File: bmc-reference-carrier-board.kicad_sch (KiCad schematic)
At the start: 0 parts

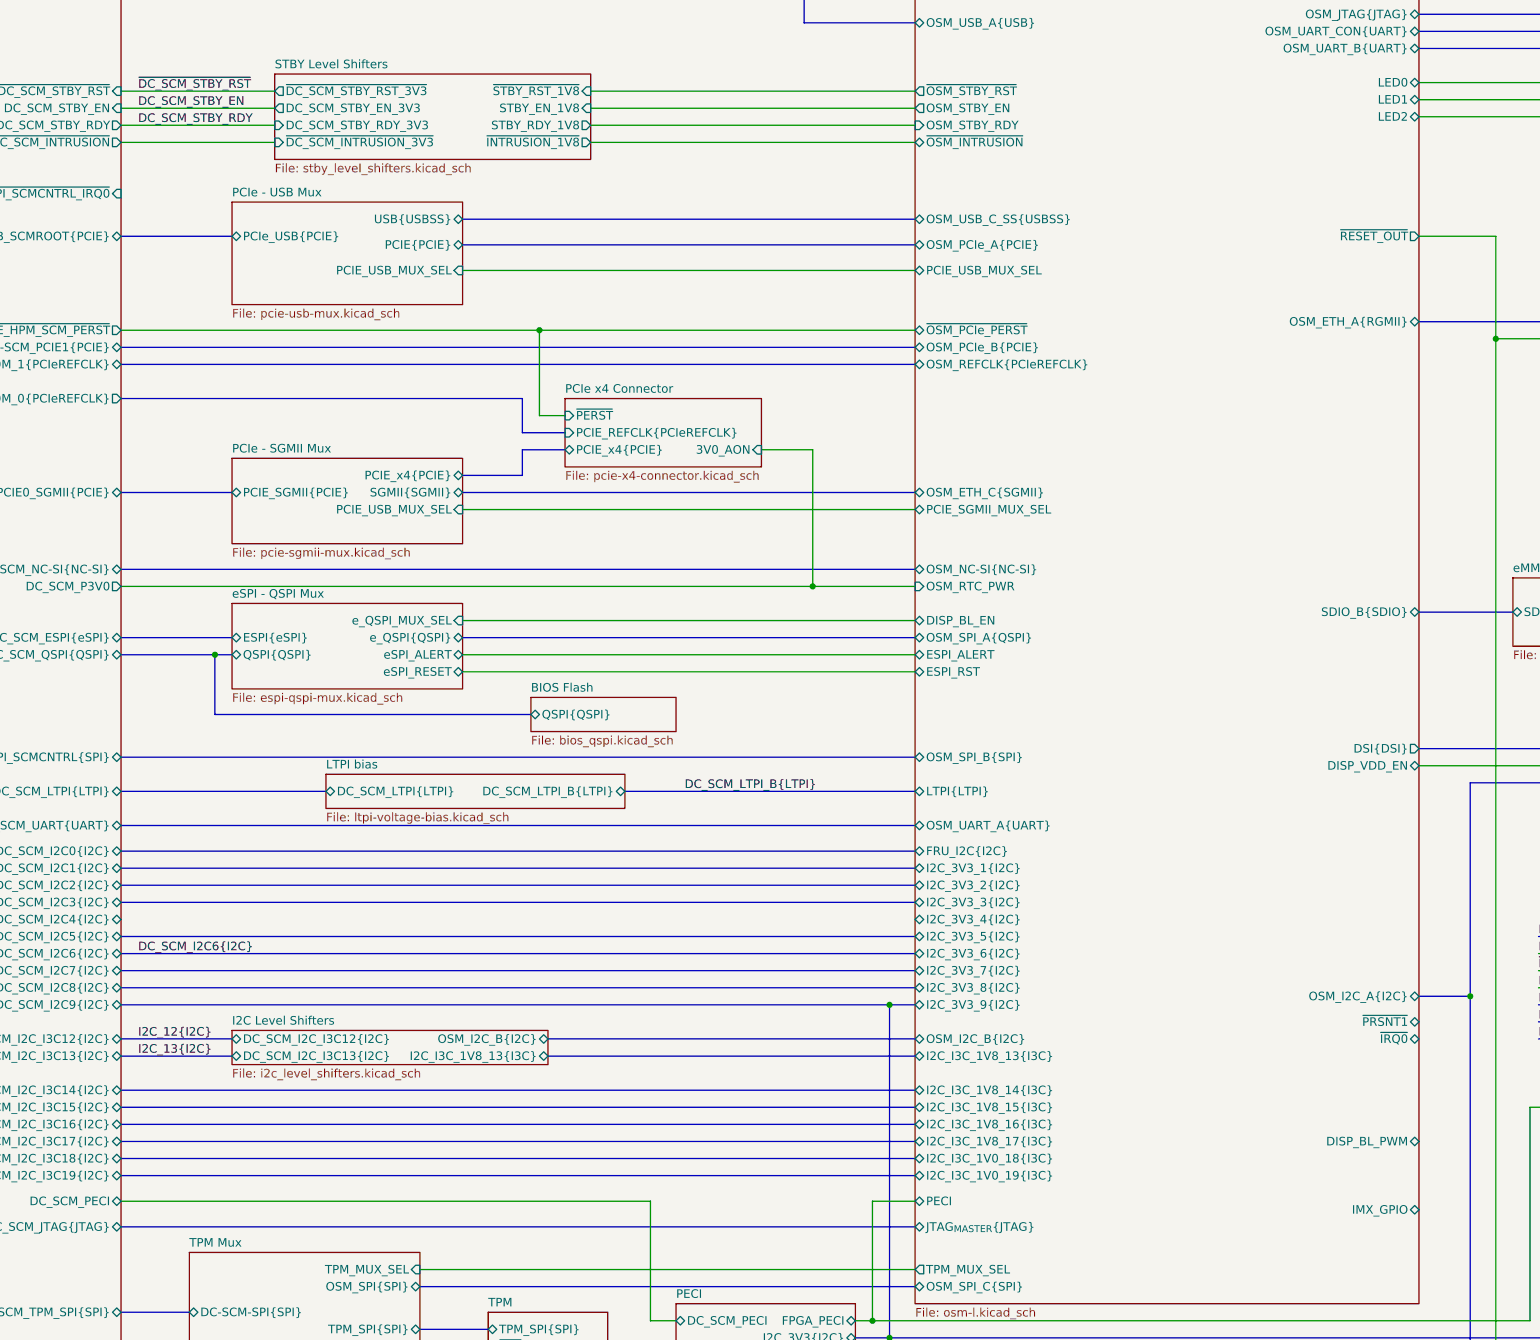
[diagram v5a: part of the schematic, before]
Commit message: [#83609] Add power pushbutton
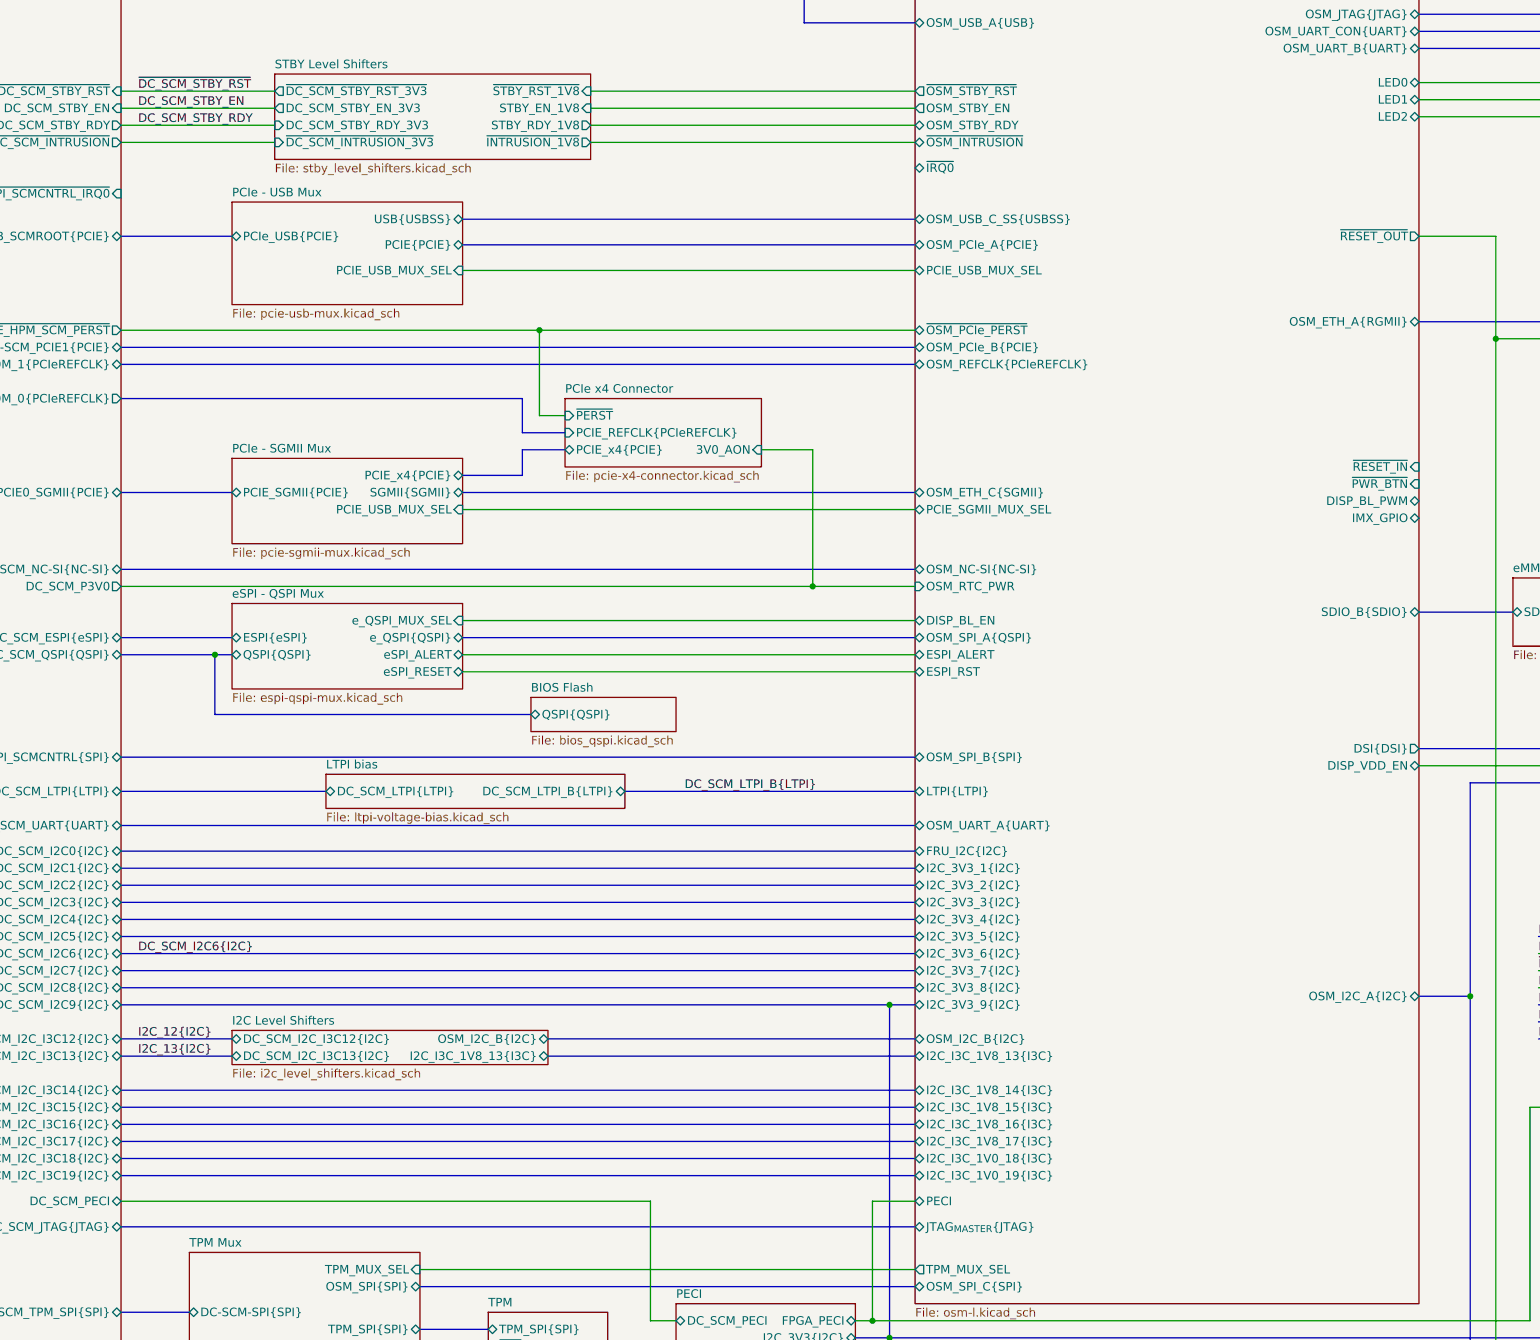
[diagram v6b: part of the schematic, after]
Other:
- sheet OSM L ports: added ~{PWR_BTN}, ~{RESET_IN}; removed ~{PRSNT1}
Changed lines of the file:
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@@
+	(bus
+		(pts
+			(xy 58.42 212.09) (xy 176.53 212.09)
+		)
+		(stroke
+			(width 0)
+			(type default)
+		)
+	)
 	(bus
 		(pts
@@
 			)
 		)
-		(pin "OSM_STBY_RDY" input
-			(at 176.53 93.98 180)
-			(effects
-				(font
-					(size 1.27 1.27)
-				)
-				(justify left)
-			)
-		)
 		(pin "~{OSM_INTRUSION}" bidirectional
 			(at 176.53 96.52 180)
@@
 		)
 		(pin "DISP_BL_PWM" bidirectional
-			(at 251.46 245.11 0)
+			(at 251.46 149.86 0)
 			(effects
 				(font
@@
 		)
 		(pin "IMX_GPIO" bidirectional
-			(at 251.46 255.27 0)
+			(at 251.46 152.4 0)
 			(effects
 				(font
@@
 		)
 		(pin "~{IRQ0}" bidirectional
-			(at 251.46 229.87 0)
-			(effects
-				(font
-					(size 1.27 1.27)
-				)
-				(justify right)
-			)
-		)
-		(pin "~{PRSNT1}" bidirectional
-			(at 251.46 227.33 0)
-			(effects
-				(font
-					(size 1.27 1.27)
-				)
-				(justify right)
+			(at 176.53 100.33 180)
+			(effects
+				(font
+					(size 1.27 1.27)
+				)
+				(justify left)
 			)
 		)
@@
 			(effects
 				(font
+					(size 1.27 1.27)
+				)
+				(justify right)
+			)
+		)
+		(pin "~{PWR_BTN}" input
+			(at 251.46 147.32 0)
+			(effects
+				(font
+					(size 1.27 1.27)
+				)
+				(justify right)
+			)
+		)
+		(pin "OSM_STBY_RDY" bidirectional
+			(at 176.53 93.98 180)
+			(effects
+				(font
+					(size 1.27 1.27)
+				)
+				(justify left)
+			)
+		)
+		(pin "~{RESET_IN}" input
+			(at 251.46 144.78 0)
+			(effects
+				(font

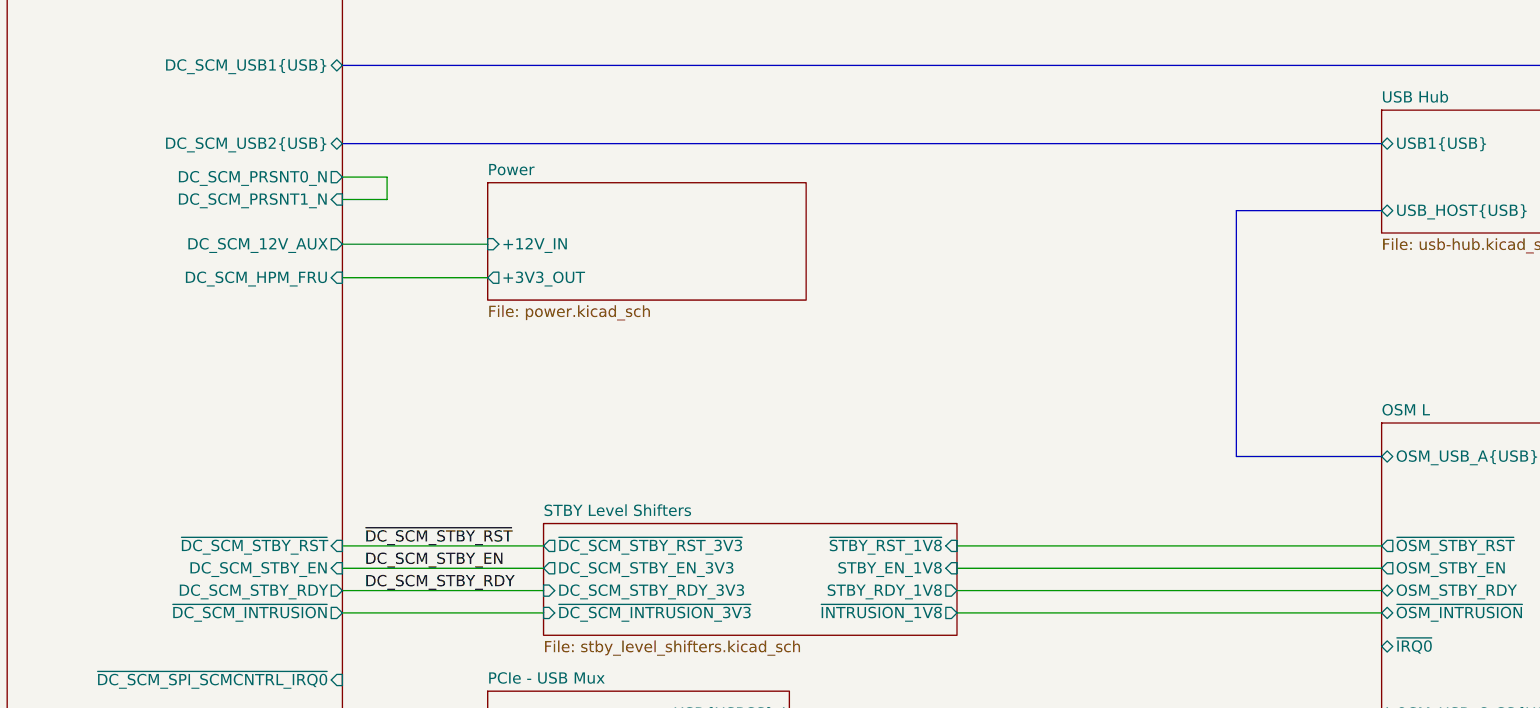
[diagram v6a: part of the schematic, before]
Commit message: [#83609] Connect PWR_EN signal, change eMMC power to AON, minor schematic refactor
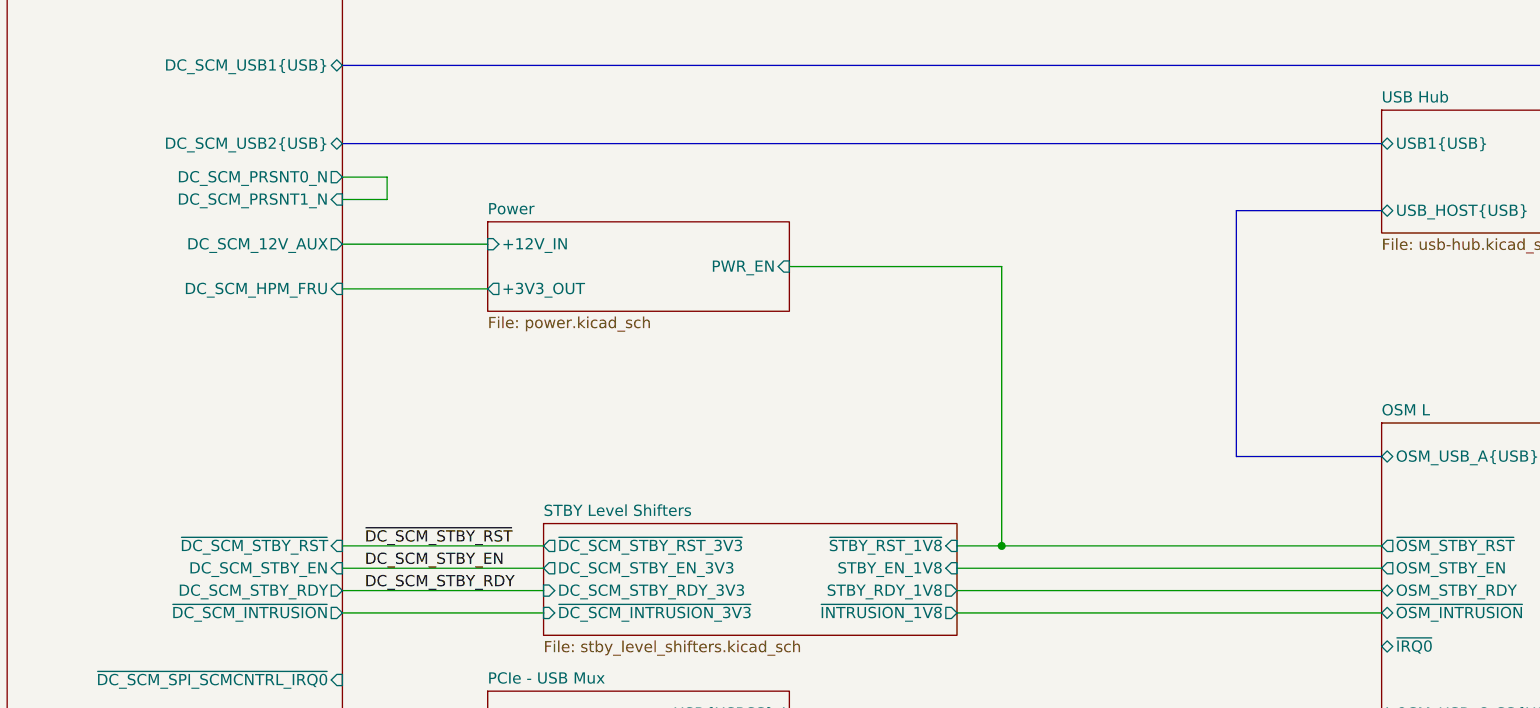
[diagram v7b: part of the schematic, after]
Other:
- sheet Power ports: added PWR_EN; removed none
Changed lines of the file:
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@@
 	)
 	(junction
+		(at 133.35 88.9)
+		(diameter 0)
+		(color 0 0 0 0)
+	)
+	(junction
 		(at 172.72 224.79)
 		(diameter 0)
@@
 		)
 	)
-	(bus
+	(wire
 		(pts
-			(xy 58.42 170.18) (xy 74.93 170.18)
+			(xy 109.22 57.15) (xy 133.35 57.15)
 		)
 		(stroke
@@
 		)
 	)
-	(wire
+	(bus
 		(pts
-			(xy 302.26 90.17) (xy 251.46 90.17)
+			(xy 58.42 170.18) (xy 74.93 170.18)
 		)
 		(stroke
@@
 	(wire
 		(pts
-			(xy 58.42 58.42) (xy 74.93 58.42)
+			(xy 302.26 90.17) (xy 251.46 90.17)
 		)
 		(stroke
@@
 		)
 	)
+	(wire
+		(pts
+			(xy 133.35 88.9) (xy 176.53 88.9)
+		)
+		(stroke
+			(width 0)
+			(type default)
+		)
+	)
 	(bus
 		(pts
@@
 	(wire
 		(pts
-			(xy 128.27 88.9) (xy 176.53 88.9)
+			(xy 128.27 88.9) (xy 133.35 88.9)
 		)
 		(stroke
@@
 		)
 	)
+	(wire
+		(pts
+			(xy 133.35 57.15) (xy 133.35 88.9)
+		)
+		(stroke
+			(width 0)
+			(type default)
+		)
+	)
+	(wire
+		(pts
+			(xy 58.42 59.69) (xy 74.93 59.69)
+		)
+		(stroke
+			(width 0)
+			(type default)
+		)
+	)
 	(bus
 		(pts
@@
 	)
 	(sheet
-		(at 74.93 47.625)
-		(size 36.195 13.335)
+		(at 74.93 52.07)
+		(size 34.29 10.16)
 		(exclude_from_sim no)
 		(in_bom yes)
@@
 		)
 		(property "Sheetname" "Power"
-			(at 74.93 46.9134 0)
+			(at 74.93 51.3584 0)
 			(effects
 				(font
@@
 		)
 		(property "Sheetfile" "power.kicad_sch"
-			(at 74.93 61.5446 0)
+			(at 74.93 62.8146 0)
 			(effects
 				(font
@@
 		)
 		(pin "+3V3_OUT" output
-			(at 74.93 58.42 180)
+			(at 74.93 59.69 180)
 			(effects
 				(font
@@
 			)
 		)
+		(pin "PWR_EN" input
+			(at 109.22 57.15 0)
+			(effects
+				(font
+					(size 1.27 1.27)
+				)
+				(justify right)
+			)
+		)
 		(instances
 			(project "bmc-reference-carrier-board"
@@
 		)
 		(pin "DC_SCM_HPM_FRU" input
-			(at 58.42 58.42 0)
+			(at 58.42 59.69 0)
 			(effects
 				(font

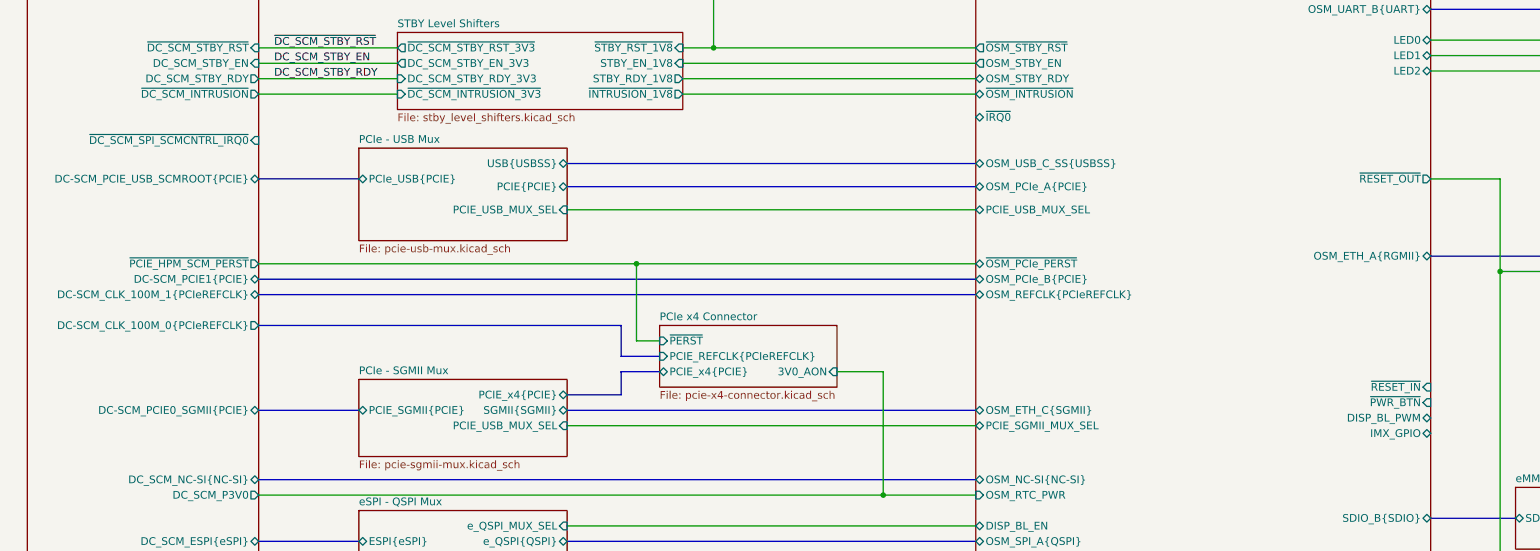
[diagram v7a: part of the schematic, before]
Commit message: [#83609] Connect all OSM signals
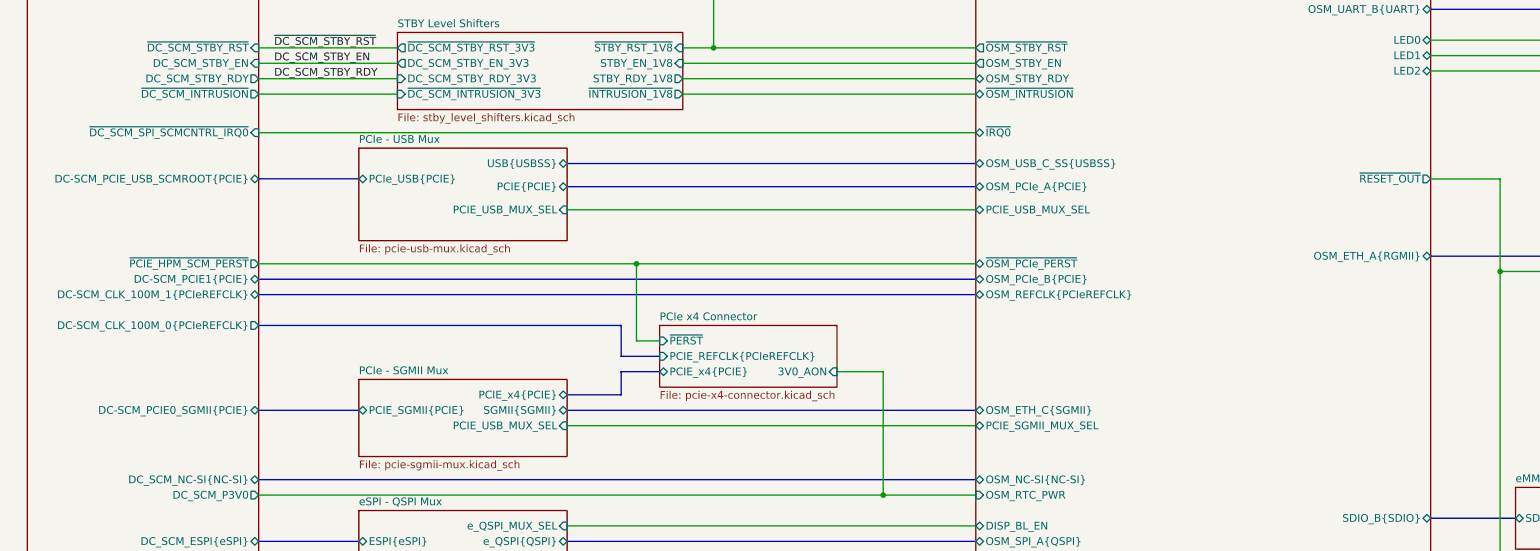
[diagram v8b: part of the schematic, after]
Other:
- sheet OSM L ports: added none; removed DISP_BL_PWM, IMX_GPIO, ~{PWR_BTN}, ~{RESET_IN}
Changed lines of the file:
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@@
+	(wire
+		(pts
+			(xy 58.42 102.87) (xy 176.53 102.87)
+		)
+		(stroke
+			(width 0)
+			(type default)
+		)
+	)
 	(wire
 		(pts
@@
 			)
 		)
-		(pin "DISP_BL_PWM" bidirectional
-			(at 251.46 149.86 0)
-			(effects
-				(font
-					(size 1.27 1.27)
-				)
-				(justify right)
-			)
-		)
 		(pin "DISP_VDD_EN" bidirectional
 			(at 251.46 189.23 0)
@@
 			)
 		)
-		(pin "IMX_GPIO" bidirectional
-			(at 251.46 152.4 0)
-			(effects
-				(font
-					(size 1.27 1.27)
-				)
-				(justify right)
-			)
-		)
 		(pin "LED0" bidirectional
 			(at 251.46 87.63 0)
@@
 		)
 		(pin "~{IRQ0}" bidirectional
-			(at 176.53 100.33 180)
+			(at 176.53 102.87 180)
 			(effects
 				(font
@@
 			)
 		)
-		(pin "~{PWR_BTN}" input
-			(at 251.46 147.32 0)
-			(effects
-				(font
-					(size 1.27 1.27)
-				)
-				(justify right)
-			)
-		)
 		(pin "OSM_STBY_RDY" bidirectional
 			(at 176.53 93.98 180)
@@
 				)
 				(justify left)
-			)
-		)
-		(pin "~{RESET_IN}" input
-			(at 251.46 144.78 0)
-			(effects
-				(font
-					(size 1.27 1.27)
-				)
-				(justify right)
 			)
 		)
@@
 		)
 		(pin "~{DC_SCM_SPI_SCMCNTRL_IRQ0}" input
-			(at 58.42 104.14 0)
-			(effects
-				(font
+			(at 58.42 102.87 0)
+			(effects
+				(font
